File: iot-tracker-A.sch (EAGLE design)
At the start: 27 parts, among them IC1 PCF85263ATL_AX, U1 ESP-WROOM-02, U2 TPL5111DDCR, U3 TPS61021ADSGR, Y1 FC-135_32.7680KA-AG3

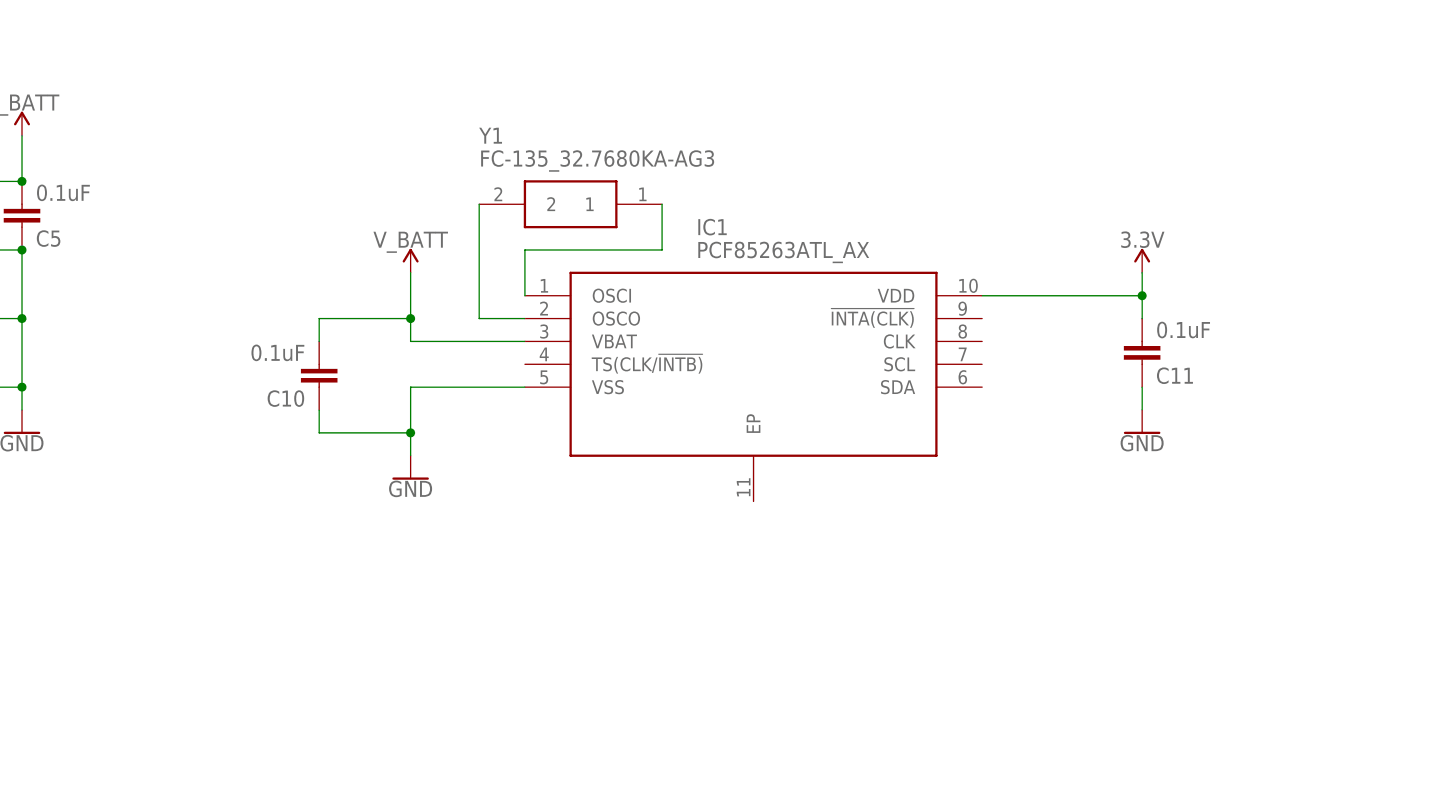
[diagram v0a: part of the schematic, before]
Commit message: Changed crystal device and added the PNP for DRVN
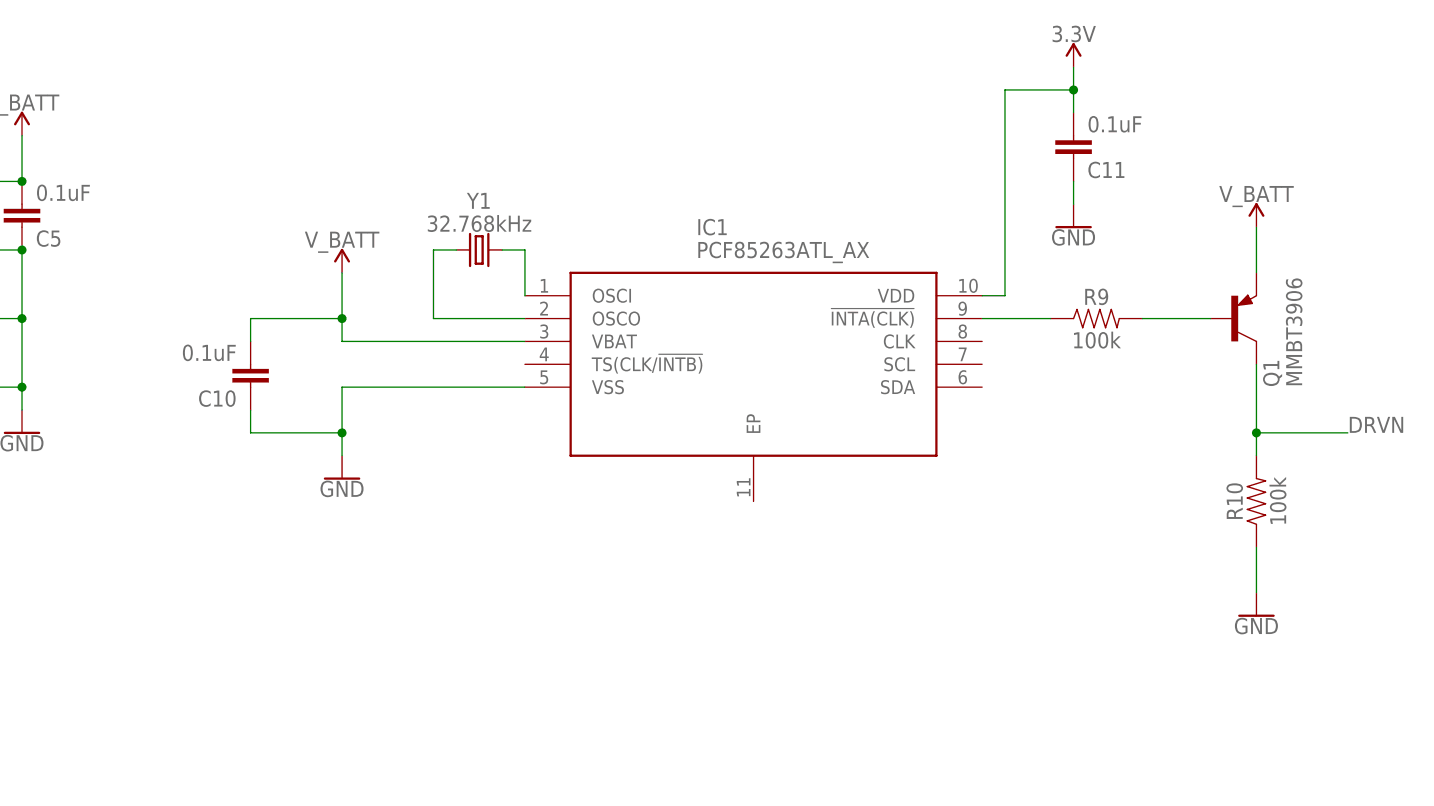
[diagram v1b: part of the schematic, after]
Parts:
- added Q1: MMBT3906, transistor-pnp:MMBT3906LT1SMD
- added R10, R9: 100k, SparkFun-Resistors:100KOHM-0603-1/10W-1%
- Y1: value FC-135_32.7680KA-AG3 -> 32.768kHz; device IOT-Tracker-A:FC-135_32.7680KA-AG3 -> SparkFun-Clocks:CRYSTAL-32.768KHZSMD-3.2X1.5
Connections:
- removed net OSCI: IC1.OSCI, Y1.1
- new net N$1: IC1.!INTA(CLK), R9.1
- new net N$2: Q1.B, R9.2
- new net N$3: IC1.OSCI, Y1.2
- net DRVN: now also Q1.C, R10.2
- net GND: now also R10.1
- net OSCO: now also Y1.1; no longer Y1.2
- net V_BATT: now also Q1.E
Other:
- moved on the sheet: C10, C11

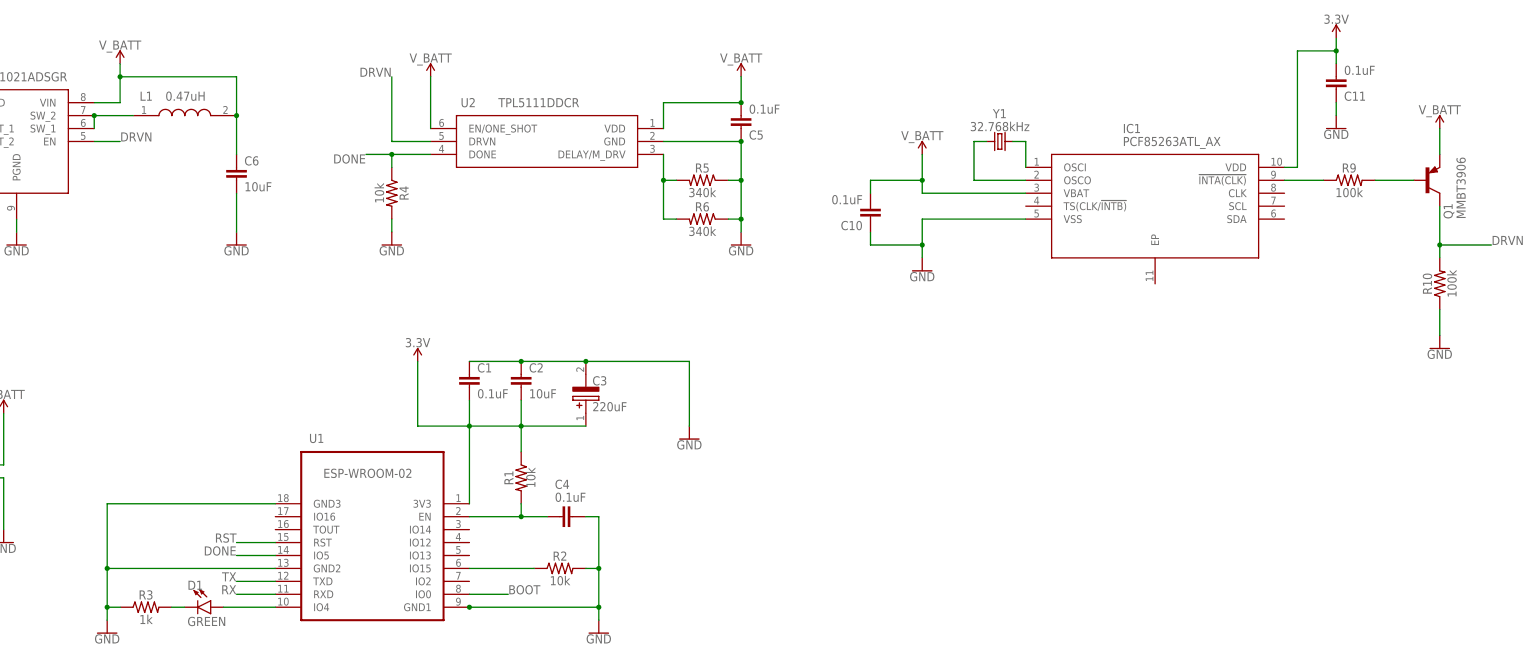
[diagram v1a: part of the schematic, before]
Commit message: Fully integrated RTC into the schematic
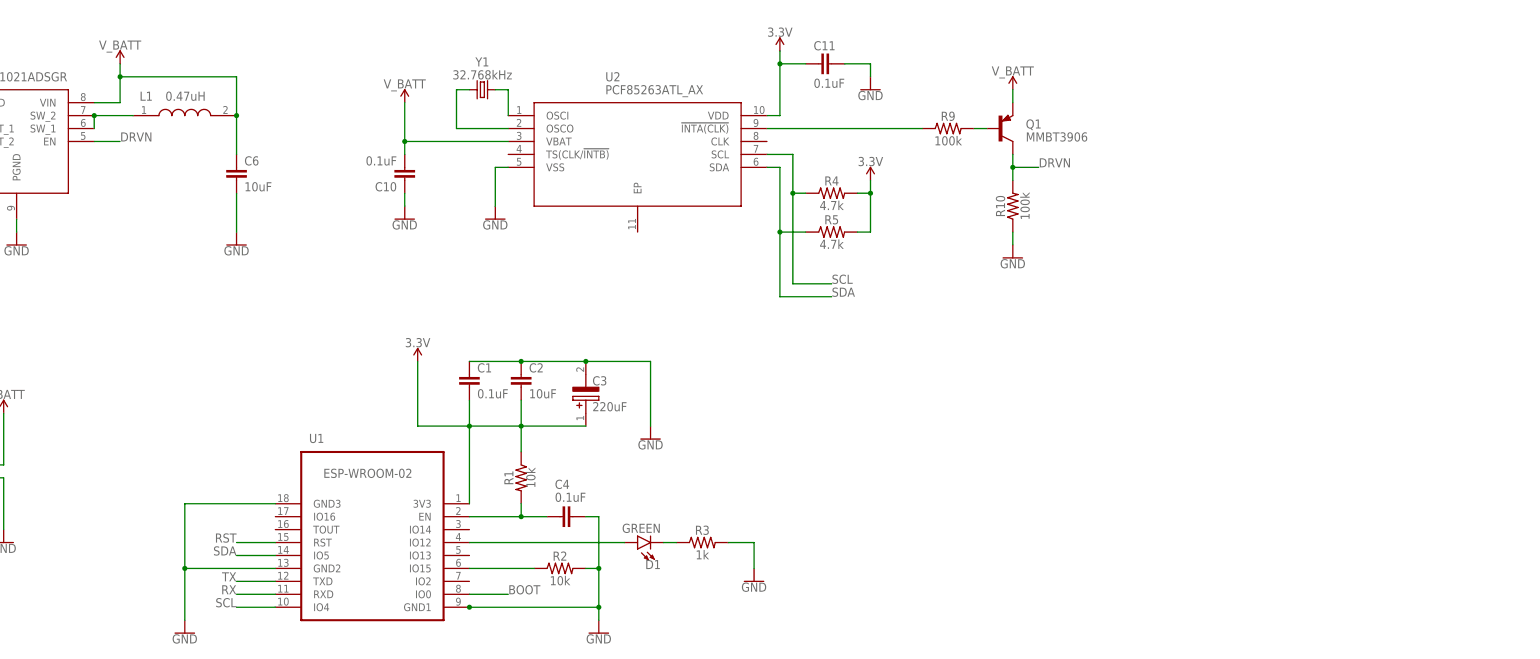
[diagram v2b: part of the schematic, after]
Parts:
- removed C5: 0.1uF, SparkFun-Capacitors:0.1UF-0603-25V-(+80/-20%)
- removed IC1: PCF85263ATL_AX, IOT-Tracker-A:PCF85263ATL_AX
- removed R6: 340k, SparkFun-Resistors:330KOHM-0603-1/10W-1%
- R4: value 10k -> 4.7k; device SparkFun-Resistors:10KOHM-0603-1/10W-1% -> SparkFun-Resistors:4.7KOHM-0603-1/10W-1%
- R5: value 340k -> 4.7k; device SparkFun-Resistors:330KOHM-0603-1/10W-1% -> SparkFun-Resistors:4.7KOHM-0603-1/10W-1%
- U2: value TPL5111DDCR -> PCF85263ATL_AX; device TPL5111DDCR:TPL5111DDCR -> IOT-Tracker-A:PCF85263ATL_AX
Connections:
- removed net DELAY: R5.2, R6.2, U2.DELAY/M_DRV
- removed net DONE: R4.1, U1.IO5, U2.DONE
- removed net IO4_LED: D1.A, U1.IO4
- removed net LED_GND: D1.C, R3.2
- new net IO12_LED: D1.A, U1.IO12
- new net LED_CATH: D1.C, R3.1
- new net SCL: R4.1, U1.IO4, U2.SCL
- new net SDA: R5.1, U1.IO5, U2.SDA
- net 3.3V: now also R4.2, R5.2, U2.VDD; no longer IC1.VDD
- net DRVN: no longer U2.DRVN
- net GND: now also R3.2, U2.VSS; no longer C5.1, IC1.VSS, R3.1, R4.2, R5.1, R6.1, U2.GND
- net N$1: now also U2.!INTA(CLK); no longer IC1.!INTA(CLK)
- net N$3: now also U2.OSCI; no longer IC1.OSCI
- net OSCO: now also U2.OSCO; no longer IC1.OSCO
- net V_BATT: now also U2.VBAT; no longer C5.2, IC1.VBAT, U2.EN/ONE_SHOT, U2.VDD
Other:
- moved on the sheet: C10, C11, D1, Q1, R10, R3, R4, R5, R9, Y1

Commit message: Minor component changes and net renaming
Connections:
- net N$1 renamed INTA
- net N$2 renamed INTA_PNP_B
- net N$3 renamed OSCI
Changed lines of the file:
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@@
 </segment>
 </net>
-<net name="N$1" class="0">
+<net name="INTA" class="0">
 <segment>
 <pinref part="R9" gate="G$1" pin="1"/>
@@
 </segment>
 </net>
-<net name="N$3" class="0">
+<net name="OSCI" class="0">
 <segment>
 <pinref part="U2" gate="G$1" pin="OSCI"/>
@@
 </segment>
 </net>
-<net name="N$2" class="0">
+<net name="INTA_PNP_B" class="0">
 <segment>
 <pinref part="R9" gate="G$1" pin="2"/>

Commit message: Reordered names and grouped components on the board
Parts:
- removed C11: 0.1uF, SparkFun-Capacitors:0.1UF-0603-25V-(+80/-20%)
- removed R10: 100k, SparkFun-Resistors:100KOHM-0603-1/10W-1%
- added C5: 10uF, SparkFun-Capacitors:10UF-0603-6.3V-20%
- added R6: 4.7k, SparkFun-Resistors:4.7KOHM-0603-1/10W-1%
- C8: value 10uF -> 10pF; device SparkFun-Capacitors:10UF-0603-6.3V-20% -> SparkFun-Capacitors:10PF-0603-50V-5%
- C9: value 10pF -> 0.1uF; device SparkFun-Capacitors:10PF-0603-50V-5% -> SparkFun-Capacitors:0.1UF-0603-25V-(+80/-20%)
- R4: value 4.7k -> 316k; device SparkFun-Resistors:4.7KOHM-0603-1/10W-1% -> SparkFun-Resistors:300KOHM-0603-1/10W-1%
- R5: value 4.7k -> 100k; device SparkFun-Resistors:4.7KOHM-0603-1/10W-1% -> SparkFun-Resistors:100KOHM-0603-1/10W-1%
- R7: value 316k -> 4.7k; device SparkFun-Resistors:300KOHM-0603-1/10W-1% -> SparkFun-Resistors:4.7KOHM-0603-1/10W-1%
- U2: value PCF85263ATL_AX -> TPS61021ADSGR; device IOT-Tracker-A:PCF85263ATL_AX -> IOT-Tracker-A:TPS61021ADSGR
- U3: value TPS61021ADSGR -> PCF85263ATL_AX; device IOT-Tracker-A:TPS61021ADSGR -> IOT-Tracker-A:PCF85263ATL_AX
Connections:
- net 3.3V: now also C10.2, C6.1, C8.2, R4.1, R6.2, R7.2, U2.VOUT_1, U2.VOUT_2, U3.VDD; no longer C11.2, C8.1, C9.2, R4.2, R5.2, R7.1, U2.VDD, U3.VOUT_1, U3.VOUT_2
- net DRVN: now also R9.2, U2.EN; no longer R10.2, U3.EN
- net FB: now also C8.1, R4.2, R5.1, U2.FB; no longer C9.1, R7.2, R8.1, U3.FB
- net GND: now also C5.2, C9.1, R5.2, R9.1, U2.AGND, U2.PGND, U3.VSS; no longer C11.1, C8.2, R10.1, R8.2, U2.VSS, U3.AGND, U3.PGND
- net INTA: now also R8.1, U3.!INTA(CLK); no longer R9.1, U2.!INTA(CLK)
- net INTA_PNP_B: now also R8.2; no longer R9.2
- net OSCI: now also U3.OSCI; no longer U2.OSCI
- net OSCO: now also U3.OSCO; no longer U2.OSCO
- net SCL: now also R6.1, U3.SCL; no longer R4.1, U2.SCL
- net SDA: now also R7.1, U3.SDA; no longer R5.1, U2.SDA
- net SW: now also U2.SW_1, U2.SW_2; no longer U3.SW_1, U3.SW_2
- net V_BATT: now also C5.1, C9.2, U2.VIN, U3.VBAT; no longer C10.2, C6.1, U2.VBAT, U3.VIN
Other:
- moved on the sheet: C10, C6, C7, C8, C9, R4, R5, R7, R8, R9

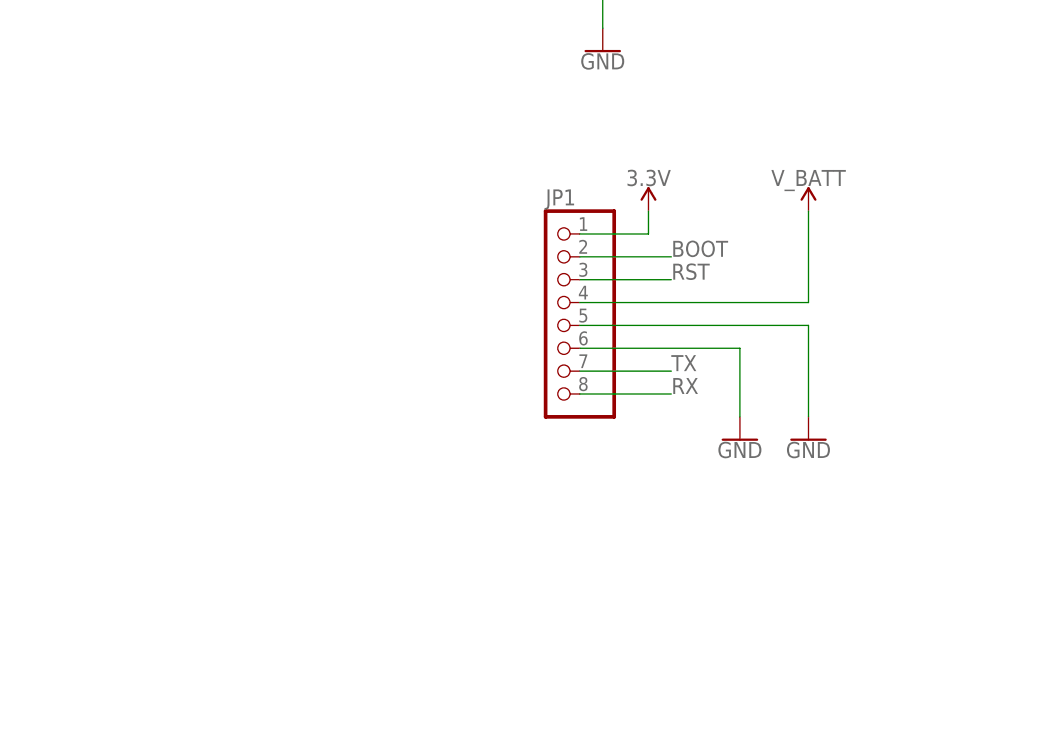
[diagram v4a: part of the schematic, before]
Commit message: Added buttons for reset and boot options
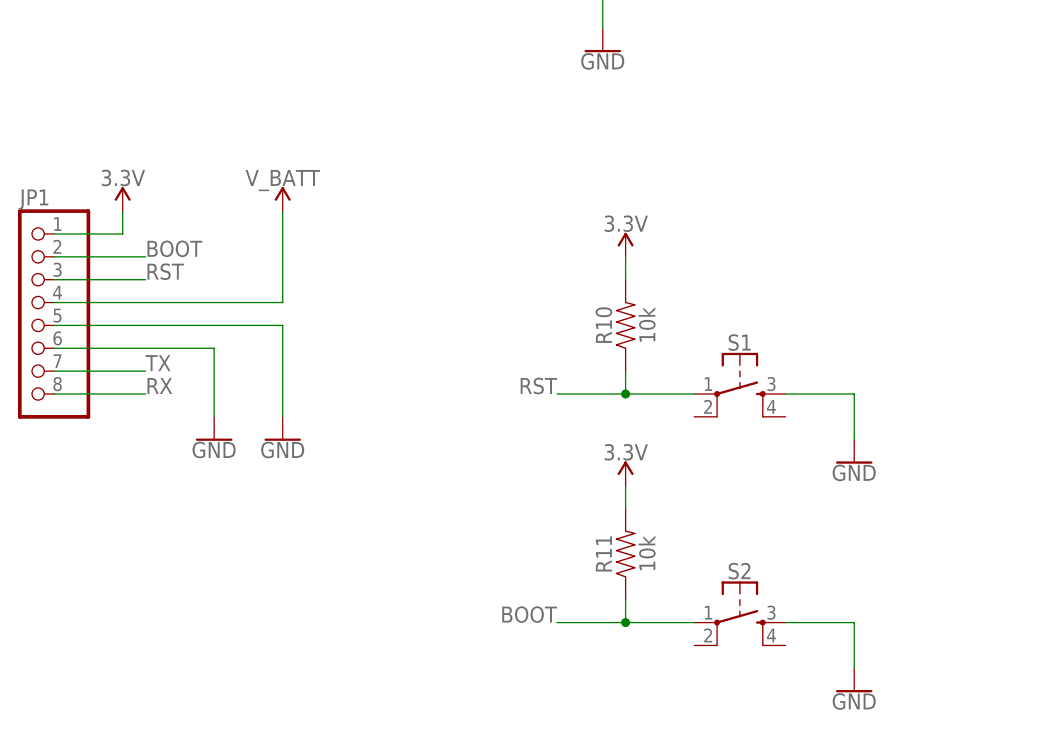
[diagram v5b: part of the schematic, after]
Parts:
- added R10, R11: 10k, SparkFun-Resistors:10KOHM-0603-1/10W-1%
- added S1, S2: (no value), SparkFun-Switches:MOMENTARY-SWITCH-SPST-2-SMD-5.2MM
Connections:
- net 3.3V: now also R10.2, R11.2
- net BOOT: now also R11.1, S2.1
- net GND: now also S1.3, S2.3
- net RST: now also R10.1, S1.1
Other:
- moved on the sheet: JP1
